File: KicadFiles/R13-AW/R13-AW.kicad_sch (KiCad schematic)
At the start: 125 parts, among them J1 Conn_01x01_Pin, J2 Conn_01x04_MountingPin, J3 Conn_01x04_MountingPin, SW1 SW_DPST_x2, SW2 SW_DPST_x2, U1 TPD4E05U06DQAR, U2 STM32F072CBTx, U3 XC6206PxxxMR

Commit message: Add and update KiCad design assets for R12/R13 variants
- refresh existing R12-AW, R13-AH, and R13-BW project files
- add the R13-AW project and variant-specific placer configs
- add 12u/13u outlines and normalize layout JSON filenames
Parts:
- removed D13, D37, D40, D46, D49: 1N4148WS, My-Fi Footprints:D_SOD-323_HandSoldering, symbol Device:D
- removed S35: MX_stab, My-Fi Footprints:STAB_MX_2.25u, symbol PCM_marbastlib-mx:MX_stab
- removed S44: MX_stab, My-Fi Footprints:STAB_MX_4.5u+5u+7u_tri, symbol PCM_marbastlib-mx:MX_stab
- added D34, D36, D39, D41, D47, D48, D51, D52, D53, D54: 1N4148WS, My-Fi Footprints:D_SOD-323_HandSoldering, symbol Device:D
- added MX51, MX52, MX54: MX_SW_solder, My-Fi Footprints:SW_MX_1.25u, symbol PCM_marbastlib-mx:MX_SW_solder
- added MX53: MX_SW_solder, My-Fi Footprints:SW_MX_1u, symbol PCM_marbastlib-mx:MX_SW_solder
- added S13: MX_stab, My-Fi Footprints:STAB_MX_2u, symbol PCM_marbastlib-mx:MX_stab
- added S39: MX_stab, My-Fi Footprints:STAB_MX_2.25u, symbol PCM_marbastlib-mx:MX_stab
- added S48: MX_stab, My-Fi Footprints:STAB_MX_6u_3u+3u, symbol PCM_marbastlib-mx:MX_stab
- MX13, MX34, MX36, MX41, MX46, MX48, MX50: footprint My-Fi Footprints:SW_MX_1.25u -> My-Fi Footprints:SW_MX_1u
- MX15, MX44, MX45: footprint My-Fi Footprints:SW_MX_1u -> My-Fi Footprints:SW_MX_1.25u
- MX23, MX24: footprint My-Fi Footprints:SW_MX_1.75u -> My-Fi Footprints:SW_MX_1u
- MX26, MX27, MX49: footprint My-Fi Footprints:SW_MX_1u -> My-Fi Footprints:SW_MX_1.75u
- MX47: footprint My-Fi Footprints:SW_MX_1.25u -> My-Fi Footprints:SW_MX_1.75u
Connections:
- net Col0: now also MX15.1, MX27.1, MX42.1; no longer MX13.1, MX24.1, MX38.1, U2.25 (PB12)
- net Col1: now also MX16.1, MX28.1, MX43.1; no longer MX14.1, MX25.1, MX39.1, MX40.1, U2.26 (PB13)
- net Col10: now also MX25.1, MX37.1, MX38.1, MX53.1; no longer MX23.1, MX35.1, MX48.1, MX49.1, U2.4 (PC15)
- net Col11: now also MX39.1; no longer MX36.1, MX37.1, MX50.1, U2.3 (PC14)
- net Col2: now also MX17.1, MX29.1, MX44.1; no longer MX15.1, MX26.1, MX41.1, MX42.1, U2.27 (PB14)
- net Col3: now also MX18.1, MX30.1, MX45.1; no longer MX16.1, MX27.1, U2.22 (PB11)
- net Col4: now also MX19.1, MX31.1, MX46.1, MX47.1; no longer MX17.1, MX28.1, MX43.1, U2.17 (PA7)
- net Col5: now also MX20.1, MX32.1, MX48.1; no longer MX18.1, MX29.1, U2.16 (PA6)
- net Col6: now also MX21.1, MX33.1; no longer MX19.1, MX30.1, MX44.1, U2.15 (PA5)
- net Col7: now also MX22.1, MX34.1, MX49.1, MX50.1; no longer MX20.1, MX31.1, MX45.1, U2.14 (PA4)
- net Col8: now also MX23.1, MX35.1, MX51.1; no longer MX21.1, MX32.1, MX46.1, MX47.1, U2.13 (PA3)
- net Col9: now also MX24.1, MX36.1, MX52.1; no longer MX22.1, MX33.1, MX34.1, U2.12 (PA2)
- net Row0: now also D14.1 (K); no longer U2.37 (PA14)
- net Row1: now also D24.1 (K), D25.1 (K), D26.1 (K); no longer D14.1 (K), U2.21 (PB10)
- net Row2: now also D38.1 (K), D34.1 (K), D36.1 (K), D39.1 (K), D41.1 (K); no longer D24.1 (K), D25.1 (K), D26.1 (K), U2.11 (PA1)
- net Row3: now also D47.1 (K), D48.1 (K), D51.1 (K), D52.1 (K), D53.1 (K), D54.1 (K); no longer D38.1 (K), U2.10 (PA0)
- net at D42.2 (A), MX42.2: no longer MX41.2
- net at D14.2 (A), MX14.2: now also MX13.2
- net at MX49.2: now also D50.2 (A), MX50.2; no longer MX48.2
- net at MX46.2, MX47.2: now also D47.2 (A)
- net at MX39.2: now also D39.2 (A); no longer MX40.2
- net at MX37.2: now also D38.2 (A), MX38.2; no longer MX36.2
- net at D33.2 (A), MX33.2: no longer MX34.2
- new net: D53.2 (A), MX53.2
- new net: D52.2 (A), MX52.2
- new net: D36.2 (A), MX36.2
- new net: D41.2 (A), MX40.2, MX41.2
- new net: D34.2 (A), MX34.2
- new net: D54.2 (A), MX54.2
- new net: D48.2 (A), MX48.2
- new net: D51.2 (A), MX51.2
- new net Col12: MX13.1, MX14.1, MX26.1, MX40.1, MX41.1, MX54.1
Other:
- title: R12-AW -> (none)
- moved on the sheet: C1, C2, C3, C4, C5, C6, C7, C8, C9, D1, D201, F1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

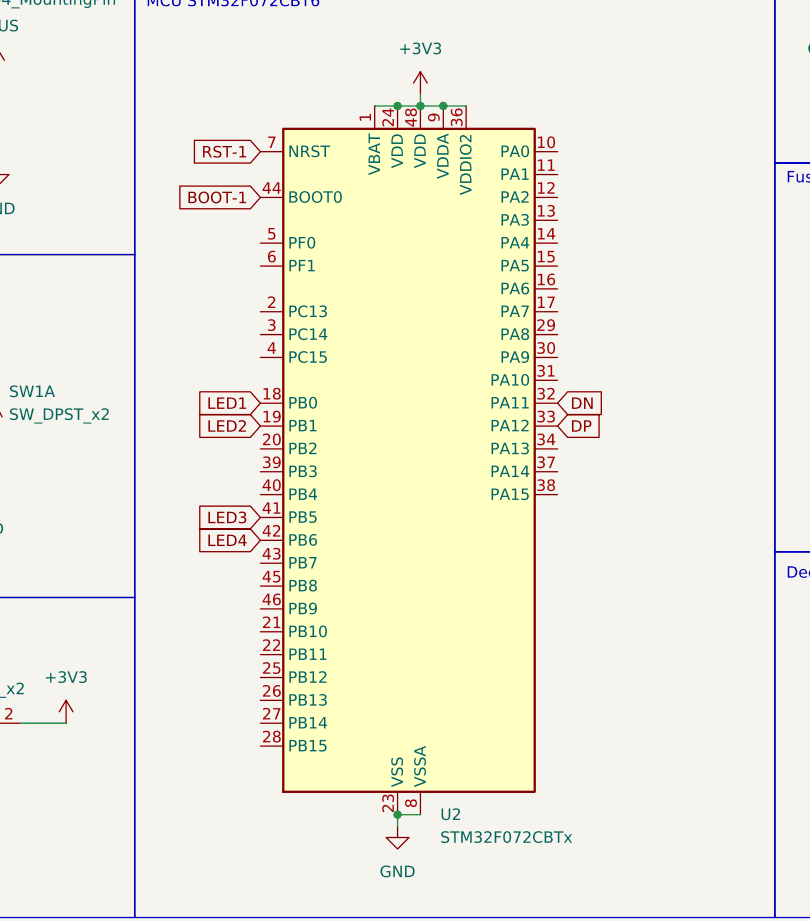
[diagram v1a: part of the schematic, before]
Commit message: Update design rules and add global labels in schematic
- Changed design rule settings in R13-AW.kicad_pro to ignore several warnings and errors, including courtyard overlaps, hole clearance, silk edge clearance, and solder mask bridges.
- Added multiple global labels in R13-AW.kicad_sch for better intersheet referencing, including Col0, Col1, Col2, Col3, Col4, Col5, Col6, Col7, Col8, Col9, Col10, Col11, Col12, Row0, Row1, Row2, and Row3.
- Ensured proper placement and formatting for new global labels to enhance readability and maintainability of the schematic.
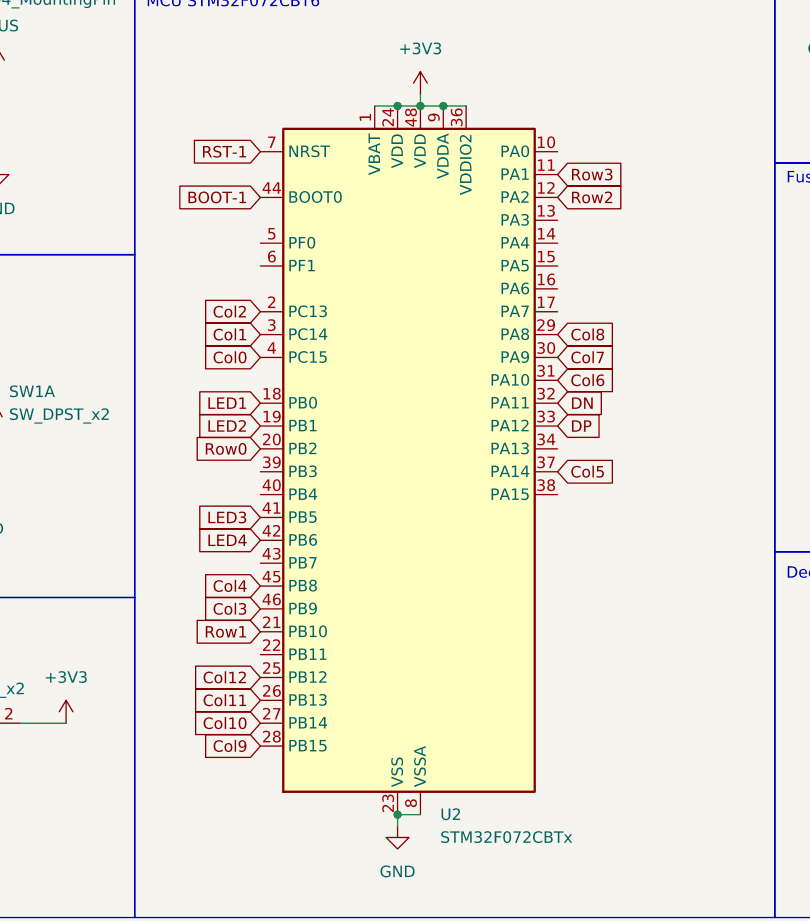
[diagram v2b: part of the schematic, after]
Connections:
- net Col0: now also U2.4 (PC15)
- net Col1: now also U2.3 (PC14)
- net Col10: now also U2.27 (PB14)
- net Col11: now also U2.26 (PB13)
- net Col12: now also U2.25 (PB12)
- net Col2: now also U2.2 (PC13)
- net Col3: now also U2.46 (PB9)
- net Col4: now also U2.45 (PB8)
- net Col5: now also U2.37 (PA14)
- net Col6: now also U2.31 (PA10)
- net Col7: now also U2.30 (PA9)
- net Col8: now also U2.29 (PA8)
- net Col9: now also U2.28 (PB15)
- net Row0: now also U2.20 (PB2)
- net Row1: now also U2.21 (PB10)
- net Row2: now also U2.12 (PA2)
- net Row3: now also U2.11 (PA1)
